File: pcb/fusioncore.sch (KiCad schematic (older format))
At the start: 116 parts, among them J1 40HAT, J10 Pump_Misc_1, J11 Pump_Misc_2, J12 I2C_DBG, J13 Conn_02x03_Top_Bottom, J14 LED, J15 Trigger, J16 WEIGHT, J17 Valve_M1, J18 Valve_M2, J19 Valve_M3, J2 Conn_02x12_Top_Bottom, J20 Valve_M4, J21 Valve_Air_Lime, J22 Valve_Air_Rum, J23 Valve_Air_Out, J3 Flow_Warm, J4 Temperature, J5 Flow_Cold, J6 WEIGHT_B, J7 Pump_Cold, J8 Pump_Warm, J9 Pump_Air, Q1 DMG2305UX, Q10 AO3400A, Q11 AO3400A, Q2 DMMT5401, Q3 AO3400A, Q4 AO3400A, Q5 AO3400A, Q6 AO3400A, Q7 AO3400A, Q8 MMBT4403, Q9 AO3400A, SW1 POWER_ON, U1 CAT24C32, U2 INA226, U3 INA226, U4 INA226, U5 TXB0108DQSR, U6 HX711, U7 P82B96

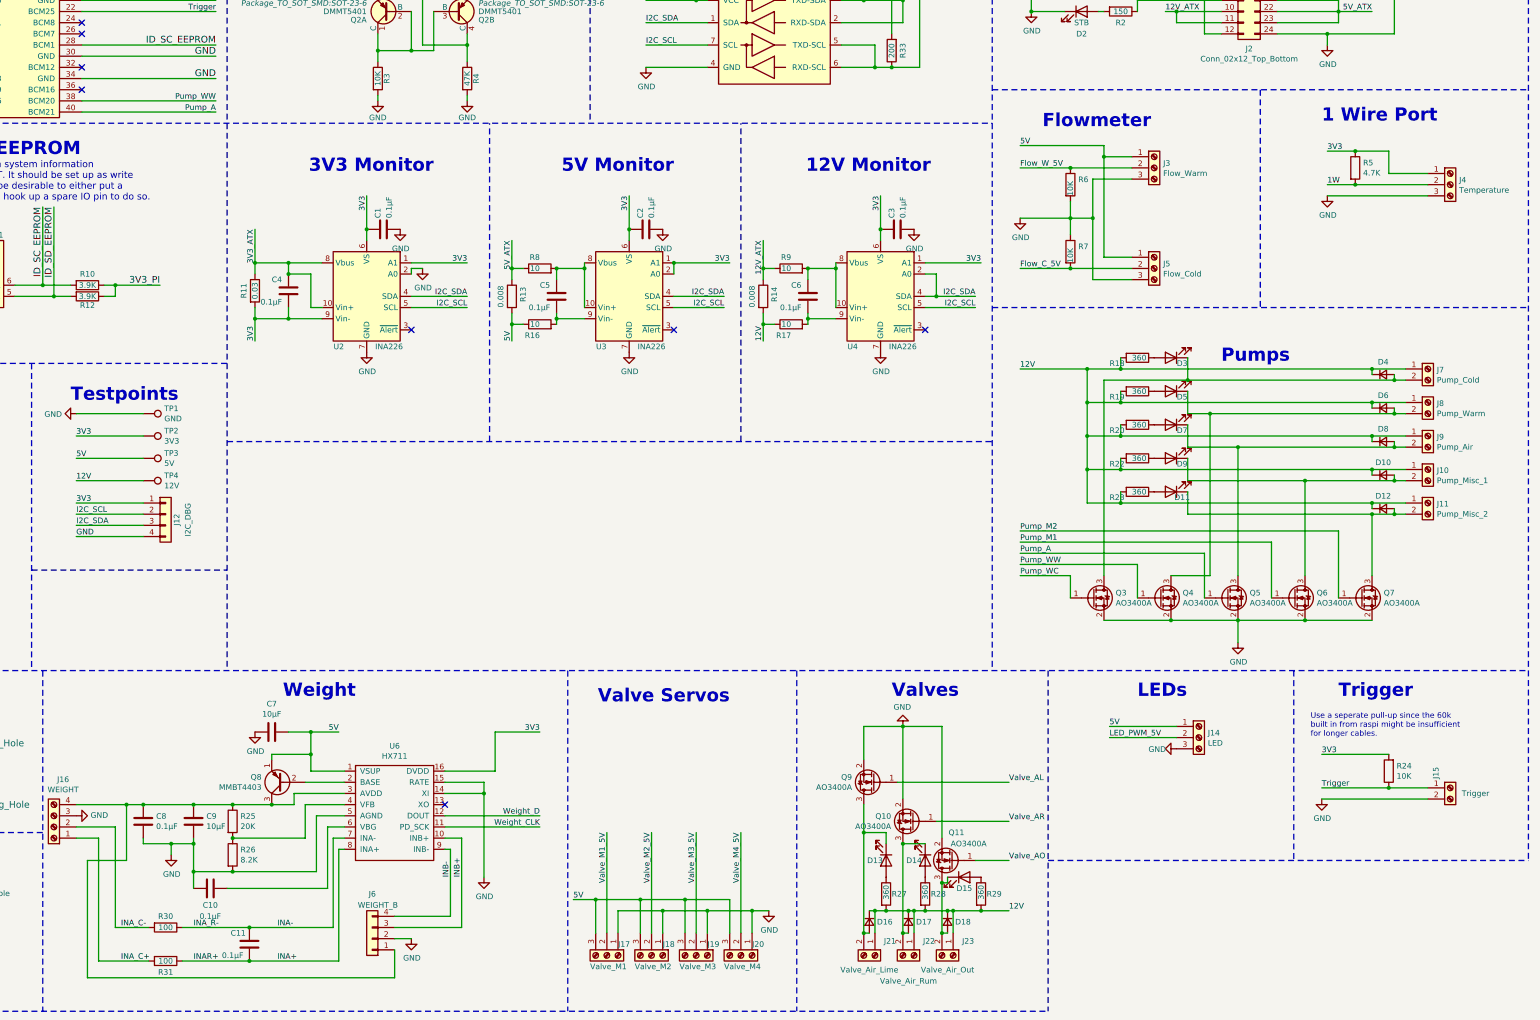
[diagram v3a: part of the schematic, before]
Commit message: Added relais for cooling compressor
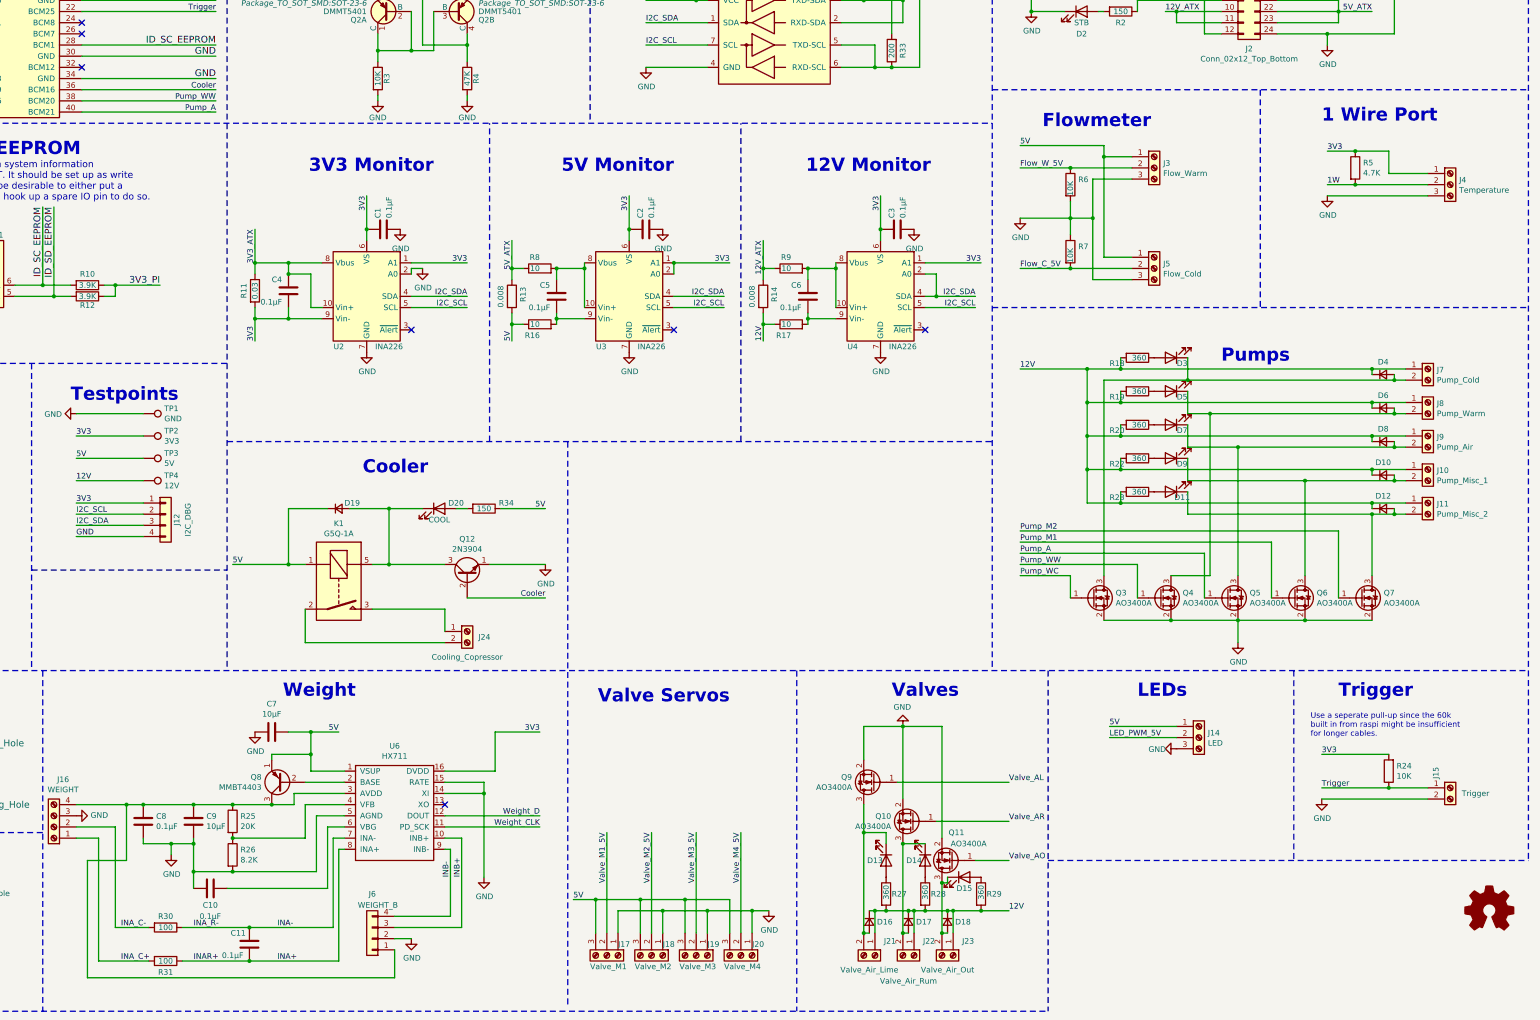
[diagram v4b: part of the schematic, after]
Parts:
- added D19: D, Diode_SMD:D_SMA, symbol Device:D_Small
- added D20: COOL, LED_SMD:LED_0805_2012Metric_Pad1.15x1.40mm_HandSolder, symbol Device:LED
- added J24: Cooling_Copressor, TerminalBlock_Phoenix:TerminalBlock_Phoenix_PT-1,5-2-5.0-H_1x02_P5.00mm_Horizontal, symbol Connector:Screw_Terminal_01x02
- added K1: G5Q-1A, Relay_THT:Relay_SPST_Omron-G5Q-1A, symbol Relay:G5Q-1A
- added Q12: 2N3904, Package_TO_SOT_SMD:SOT-23, symbol Transistor_BJT:2N3904
- added R34: 150, Resistor_SMD:R_0805_2012Metric_Pad1.15x1.40mm_HandSolder, symbol Device:R
- J15: footprint TerminalBlock_Phoenix:TerminalBlock_Phoenix_PT-1,5-2-5.0-H_1x02_P5.00mm_Horizontal -> project_footprints:TerminalBlock_Phoenix_PT-1,5-2-3.5-H_1x02_P3.50mm_Diagonal; Digikey (none) -> 277-1779-ND
- J4: footprint TerminalBlock_Phoenix:TerminalBlock_Phoenix_PT-1,5-3-5.0-H_1x03_P5.00mm_Horizontal -> project_footprints:TerminalBlock_Phoenix_PT-1,5-2-3.5-H_1x03_P3.50mm_Diagonal; Digikey (none) -> 277-1780-ND
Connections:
- net 5V: now also D19.1 (K), K1.1, R34.1
- net GND: now also Q12.1 (E)
- net Cooler: now reaches J1.36 (BCM16)
- net Cooler: now also Q12.2 (B)
- new net: J24.1 (Pin_1), K1.3
- new net: J24.2 (Pin_2), K1.2
- new net: D19.2 (A), D20.1 (K), K1.5, Q12.3 (C)
- new net: D20.2 (A), R34.2
- no-connect marks 13 -> 12
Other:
- note added: "Cooler"
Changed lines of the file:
@@
 F 0 "J4" H 15430 3842 50  0000 L CNN
 F 1 "Temperature" H 15430 3751 50  0000 L CNN
-F 2 "TerminalBlock_Phoenix:TerminalBlock_Phoenix_PT-1,5-3-5.0-H_1x03_P5.00mm_Horizontal" H 15350 3800 50  0001 C CNN
-F 3 "https://media.digikey.com/pdf/Data%20Sheets/Phoenix%20Contact%20PDFs/1935161.pdf" H 15350 3800 50  0001 C CNN
+F 2 "project_footprints:TerminalBlock_Phoenix_PT-1,5-2-3.5-H_1x03_P3.50mm_Diagonal" H 15350 3800 50  0001 C CNN
+F 3 "https://media.digikey.com/pdf/Data%20Sheets/Phoenix%20Contact%20PDFs/Combicon%20Compact%20Series.pdf" H 15350 3800 50  0001 C CNN
+F 4 " 277-1780-ND" H 15350 3800 50  0001 C CNN "Digikey"
 	1    15350 3800
 	1    0    0    -1
@@
 F 0 "J15" V 15222 9280 50  0000 L CNN
 F 1 "Trigger" H 15700 9150 50  0000 R CNN
-F 2 "TerminalBlock_Phoenix:TerminalBlock_Phoenix_PT-1,5-2-5.0-H_1x02_P5.00mm_Horizontal" H 15350 9200 50  0001 C CNN
-F 3 "~" H 15350 9200 50  0001 C CNN
+F 2 "project_footprints:TerminalBlock_Phoenix_PT-1,5-2-3.5-H_1x02_P3.50mm_Diagonal" H 15350 9200 50  0001 C CNN
+F 3 "https://media.digikey.com/pdf/Data%20Sheets/Phoenix%20Contact%20PDFs/Combicon%20Compact%20Series.pdf" H 15350 9200 50  0001 C CNN
+F 4 " 277-1779-ND" V 15350 9200 50  0001 C CNN "Digikey"
 	1    15350 9200
 	1    0    0    -1
@@
 	1900 2950 700  2950
 NoConn ~ 3100 2750
-NoConn ~ 3100 2950
 Wire Wire Line
 	1300 6250 1300 5900
@@
 Wire Notes Line
 	11750 9850 16050 9850
-Wire Notes Line
-	7450 8150 7450 11200
 Wire Notes Line
 	11750 8150 11750 11200
@@
 Wire Wire Line
 	3500 9350 3650 9350
+$Comp
+L Graphic:Logo_Open_Hardware_Small #LOGO1
+U 1 1 5E603C52
+P 15700 10300
+F 0 "#LOGO1" H 15700 10575 50  0001 C CNN
+F 1 "Logo_Open_Hardware_Small" H 15700 10075 50  0001 C CNN
+F 2 "" H 15700 10300 50  0001 C CNN
+F 3 "~" H 15700 10300 50  0001 C CNN
+	1    15700 10300
+	1    0    0    -1
+$EndComp
+$Comp
+L Connector:Screw_Terminal_01x02 J24
+U 1 1 5E60ECEB
+P 6550 7800
+F 0 "J24" H 6650 7750 50  0000 L CNN
+F 1 "Cooling_Copressor" H 6550 7600 50  0000 C TNN
+F 2 "TerminalBlock_Phoenix:TerminalBlock_Phoenix_PT-1,5-2-5.0-H_1x02_P5.00mm_Horizontal" H 6550 7800 50  0001 C CNN
+F 3 "https://media.digikey.com/pdf/Data%20Sheets/Phoenix%20Contact%20PDFs/1935161.pdf" H 6550 7800 50  0001 C CNN
+	1    6550 7800
+	1    0    0    -1
+$EndComp
+Wire Wire Line
+	6350 7900 5100 7900
+Wire Wire Line
+	5100 7900 5100 7600
+$Comp
+L Transistor_BJT:2N3904 Q12
+U 1 1 5E6A5955
+P 6550 7300
+F 0 "Q12" V 6878 7300 50  0000 C CNN
+F 1 "2N3904" V 6787 7300 50  0000 C CNN
+F 2 "Package_TO_SOT_SMD:SOT-23" H 6750 7225 50  0001 L CIN
+F 3 "https://datasheet.lcsc.com/szlcsc/KEC-Semicon-2N3904S-RTK-PS_C18536.pdf" H 6550 7300 50  0001 L CNN
+F 4 "C18536" H 6550 7300 50  0001 C CNN "LCSC"
+	1    6550 7300
+	0    -1   -1   0
+$EndComp
+$Comp
+L Device:D_Small D19
+U 1 1 5E6A8FA4
+P 5400 6700
+F 0 "D19" H 5450 6750 50  0000 L CNN
+F 1 "D" V 5445 6768 50  0001 L CNN
+F 2 "Diode_SMD:D_SMA" V 5400 6700 50  0001 C CNN
+F 3 "~" V 5400 6700 50  0001 C CNN
+F 4 "C22452" V 5400 6700 50  0001 C CNN "LCSC"
+	1    5400 6700
+	1    0    0    -1
+$EndComp
+Wire Wire Line
+	5700 7200 5850 7200
+Wire Wire Line
+	5850 7200 5850 6700
+Wire Wire Line
+	5850 6700 5500 6700
+Wire Wire Line
+	5100 7200 4950 7200
+Wire Wire Line
+	4950 7200 4950 6700
+Wire Wire Line
+	4950 6700 5300 6700
+Wire Wire Line
+	4950 7200 4450 7200
+Connection ~ 4950 7200
+Text Label 4450 7200 0    50   ~ 0
+5V
+Wire Wire Line
+	5850 7200 6350 7200
+Connection ~ 5850 7200
+Wire Wire Line
+	6750 7200 7250 7200
+$Comp
+L power:GND #PWR0103
+U 1 1 5E904F19
+P 7250 7200
+F 0 "#PWR0103" H 7250 6950 50  0001 C CNN
+F 1 "GND" H 7255 7027 50  0000 C CNN
+F 2 "" H 7250 7200 50  0001 C CNN
+F 3 "" H 7250 7200 50  0001 C CNN
+	1    7250 7200
+	1    0    0    -1
+$EndComp
+Wire Wire Line
+	6550 7500 7250 7500
+Text Label 7250 7500 2    50   ~ 0
+Cooler
+$Comp
+L Device:R R34
+U 1 1 5E99FEBD
+P 6700 6700
+F 0 "R34" V 6650 6900 50  0000 C CNN
+F 1 "150" V 6700 6700 50  0000 C CNN
+F 2 "Resistor_SMD:R_0805_2012Metric_Pad1.15x1.40mm_HandSolder" V 6630 6700 50  0001 C CNN
+F 3 "~" H 6700 6700 50  0001 C CNN
+F 4 "C17471" V 6700 6700 50  0001 C CNN "LCSC"
+	1    6700 6700
+	0    1    1    0
+$EndComp
+$Comp
+L Device:LED D20
+U 1 1 5E9A1CDC
+P 6300 6700
+F 0 "D20" H 6450 6750 50  0000 C CNN
+F 1 "COOL" H 6300 6600 50  0000 C CNN
+F 2 "LED_SMD:LED_0805_2012Metric_Pad1.15x1.40mm_HandSolder" H 6300 6700 50  0001 C CNN
+F 3 "~" H 6300 6700 50  0001 C CNN
+F 4 "C2296" H 6300 6700 50  0001 C CNN "LCSC"
+	1    6300 6700
+	1    0    0    -1
+$EndComp
+Wire Wire Line
+	7250 6700 6850 6700
+Wire Wire Line
+	6550 6700 6450 6700
+Wire Wire Line
+	6150 6700 5850 6700
+Connection ~ 5850 6700
+Text Label 7250 6700 2    50   ~ 0
+5V
+Wire Notes Line
+	7450 6100 7450 11150
+Text Notes 6200 6400 2    118  ~ 24
+Cooler
+$Comp
+L Relay:G5Q-1A K1
+U 1 1 5EC7061B
+P 5400 7400
+F 0 "K1" V 4833 7400 50  0000 C CNN
+F 1 "G5Q-1A" V 4924 7400 50  0000 C CNN
+F 2 "Relay_THT:Relay_SPST_Omron-G5Q-1A" H 5750 7350 50  0001 L CNN
+F 3 "https://omronfs.omron.com/en_US/ecb/products/pdf/en-g5q.pdf" H 5400 7400 50  0001 C CNN
+F 4 "Z3632-ND" V 5400 7400 50  0001 C CNN "Digikey"
+	1    5400 7400
+	0    1    1    0
+$EndComp
+Wire Wire Line
+	6350 7600 5700 7600
+Wire Wire Line
+	6350 7600 6350 7800
+Wire Wire Line
+	3100 2950 4300 2950
+Text Label 4300 2950 2    50   ~ 0
+Cooler
 $EndSCHEMATC

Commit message: Added Relais to board
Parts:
- J10, J11, J21, J22, J23, J7, J8, J9: Digikey (none) -> 277-1667-ND
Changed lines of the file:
@@
 F 2 "TerminalBlock_Phoenix:TerminalBlock_Phoenix_PT-1,5-2-5.0-H_1x02_P5.00mm_Horizontal" H 15150 5450 50  0001 C CNN
 F 3 "https://media.digikey.com/pdf/Data%20Sheets/Phoenix%20Contact%20PDFs/1935161.pdf" H 15150 5450 50  0001 C CNN
+F 4 "277-1667-ND" H 15150 5450 50  0001 C CNN "Digikey"
 	1    15150 5450
 	1    0    0    -1
@@
 F 2 "TerminalBlock_Phoenix:TerminalBlock_Phoenix_PT-1,5-2-5.0-H_1x02_P5.00mm_Horizontal" H 15150 5750 50  0001 C CNN
 F 3 "https://media.digikey.com/pdf/Data%20Sheets/Phoenix%20Contact%20PDFs/1935161.pdf" H 15150 5750 50  0001 C CNN
+F 4 "277-1667-ND" H 15150 5750 50  0001 C CNN "Digikey"
 	1    15150 5750
 	1    0    0    -1
@@
 F 2 "TerminalBlock_Phoenix:TerminalBlock_Phoenix_PT-1,5-2-5.0-H_1x02_P5.00mm_Horizontal" H 15150 6050 50  0001 C CNN
 F 3 "https://media.digikey.com/pdf/Data%20Sheets/Phoenix%20Contact%20PDFs/1935161.pdf" H 15150 6050 50  0001 C CNN
+F 4 "277-1667-ND" H 15150 6050 50  0001 C CNN "Digikey"
 	1    15150 6050
 	1    0    0    -1
@@
 F 2 "TerminalBlock_Phoenix:TerminalBlock_Phoenix_PT-1,5-2-5.0-H_1x02_P5.00mm_Horizontal" H 15150 6350 50  0001 C CNN
 F 3 "https://media.digikey.com/pdf/Data%20Sheets/Phoenix%20Contact%20PDFs/1935161.pdf" H 15150 6350 50  0001 C CNN
+F 4 "277-1667-ND" H 15150 6350 50  0001 C CNN "Digikey"
 	1    15150 6350
 	1    0    0    -1
@@
 F 2 "TerminalBlock_Phoenix:TerminalBlock_Phoenix_PT-1,5-2-5.0-H_1x02_P5.00mm_Horizontal" H 15150 6650 50  0001 C CNN
 F 3 "https://media.digikey.com/pdf/Data%20Sheets/Phoenix%20Contact%20PDFs/1935161.pdf" H 15150 6650 50  0001 C CNN
+F 4 "277-1667-ND" H 15150 6650 50  0001 C CNN "Digikey"
 	1    15150 6650
 	1    0    0    -1
@@
 F 2 "TerminalBlock_Phoenix:TerminalBlock_Phoenix_PT-1,5-2-5.0-H_1x02_P5.00mm_Horizontal" H 10900 10700 50  0001 C CNN
 F 3 "https://media.digikey.com/pdf/Data%20Sheets/Phoenix%20Contact%20PDFs/1935161.pdf" H 10900 10700 50  0001 C CNN
+F 4 "277-1667-ND" V 10900 10700 50  0001 C CNN "Digikey"
 	1    10900 10700
 	0    1    1    0
@@
 F 2 "TerminalBlock_Phoenix:TerminalBlock_Phoenix_PT-1,5-2-5.0-H_1x02_P5.00mm_Horizontal" H 10550 10700 50  0001 C CNN
 F 3 "https://media.digikey.com/pdf/Data%20Sheets/Phoenix%20Contact%20PDFs/1935161.pdf" H 10550 10700 50  0001 C CNN
+F 4 "277-1667-ND" V 10550 10700 50  0001 C CNN "Digikey"
 	1    10550 10700
 	0    1    1    0
@@
 F 2 "TerminalBlock_Phoenix:TerminalBlock_Phoenix_PT-1,5-2-5.0-H_1x02_P5.00mm_Horizontal" H 10200 10700 50  0001 C CNN
 F 3 "https://media.digikey.com/pdf/Data%20Sheets/Phoenix%20Contact%20PDFs/1935161.pdf" H 10200 10700 50  0001 C CNN
+F 4 "277-1667-ND" V 10200 10700 50  0001 C CNN "Digikey"
 	1    10200 10700
 	0    1    1    0

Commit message: Added and moved some capacitors
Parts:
- added C12, C13, C14: 0.1μF, Capacitor_SMD:C_0805_2012Metric_Pad1.15x1.40mm_HandSolder, symbol Device:C
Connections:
- net 3V3: now also C13.2, C14.1
- net 5V: now also C12.2
- net GND: now also C12.1, C13.1, C14.2
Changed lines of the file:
@@
 NoConn ~ 3100 2750
 Wire Wire Line
-	1300 6250 1300 5900
-Wire Wire Line
-	1500 6250 1500 5900
+	1300 6250 1300 6200
 Text Label 1300 5900 3    50   ~ 0
 3V3
@@
 	1    0    0    -1
 $EndComp
-Wire Wire Line
-	1000 6250 1000 5900
 Connection ~ 1000 6250
 Text Label 1000 5900 3    50   ~ 0
@@
 Text Label 4300 2950 2    50   ~ 0
 Cooler
+$Comp
+L Device:C C12
+U 1 1 5E7BF599
+P 2100 6100
+F 0 "C12" V 2050 6250 50  0000 R CNN
+F 1 "0.1μF" V 2150 6400 50  0000 R CNN
+F 2 "Capacitor_SMD:C_0805_2012Metric_Pad1.15x1.40mm_HandSolder" H 2138 5950 50  0001 C CNN
+F 3 "~" H 2100 6100 50  0001 C CNN
+F 4 "C49678" H 2100 6100 50  0001 C CNN "LCSC"
+	1    2100 6100
+	0    1    1    0
+$EndComp
+$Comp
+L Device:C C13
+U 1 1 5E869BEF
+P 2100 6350
+F 0 "C13" V 2050 6500 50  0000 R CNN
+F 1 "0.1μF" V 2150 6650 50  0000 R CNN
+F 2 "Capacitor_SMD:C_0805_2012Metric_Pad1.15x1.40mm_HandSolder" H 2138 6200 50  0001 C CNN
+F 3 "~" H 2100 6350 50  0001 C CNN
+F 4 "C49678" H 2100 6350 50  0001 C CNN "LCSC"
+	1    2100 6350
+	0    1    1    0
+$EndComp
+Wire Wire Line
+	1000 5900 1000 6250
+$Comp
+L power:GND #PWR0104
+U 1 1 5E813936
+P 2500 6350
+F 0 "#PWR0104" H 2500 6100 50  0001 C CNN
+F 1 "GND" H 2505 6177 50  0000 C CNN
+F 2 "" H 2500 6350 50  0001 C CNN
+F 3 "" H 2500 6350 50  0001 C CNN
+	1    2500 6350
+	1    0    0    -1
+$EndComp
+Wire Wire Line
+	2250 6100 2500 6100
+Wire Wire Line
+	2500 6100 2500 6350
+Wire Wire Line
+	1500 5900 1500 6100
+Wire Wire Line
+	2250 6350 2500 6350
+Connection ~ 2500 6350
+Wire Wire Line
+	1950 6100 1500 6100
+Connection ~ 1500 6100
+Wire Wire Line
+	1500 6100 1500 6250
+Wire Wire Line
+	1950 6350 1850 6350
+Wire Wire Line
+	1850 6350 1850 6200
+Wire Wire Line
+	1850 6200 1300 6200
+Connection ~ 1300 6200
+Wire Wire Line
+	1300 6200 1300 5900
+$Comp
+L Device:C C14
+U 1 1 5EA9FECD
+P 6650 8700
+F 0 "C14" V 6600 8850 50  0000 R CNN
+F 1 "0.1μF" V 6800 8850 50  0000 R CNN
+F 2 "Capacitor_SMD:C_0805_2012Metric_Pad1.15x1.40mm_HandSolder" H 6688 8550 50  0001 C CNN
+F 3 "~" H 6650 8700 50  0001 C CNN
+F 4 "C49678" H 6650 8700 50  0001 C CNN "LCSC"
+	1    6650 8700
+	0    1    1    0
+$EndComp
+Connection ~ 6800 8700
+$Comp
+L power:GND #PWR0105
+U 1 1 5EAA3D3D
+P 6400 8700
+F 0 "#PWR0105" H 6400 8450 50  0001 C CNN
+F 1 "GND" H 6405 8527 50  0000 C CNN
+F 2 "" H 6400 8700 50  0001 C CNN
+F 3 "" H 6400 8700 50  0001 C CNN
+	1    6400 8700
+	1    0    0    -1
+$EndComp
+Wire Wire Line
+	6500 8700 6400 8700
 $EndSCHEMATC

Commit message: Added LCSC for R30/R31
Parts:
- R30, R31: LCSC (none) -> C17408
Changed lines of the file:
@@
 F 2 "Resistor_SMD:R_0805_2012Metric_Pad1.15x1.40mm_HandSolder" V 3780 10450 50  0001 C CNN
 F 3 "~" H 3850 10450 50  0001 C CNN
+F 4 "C17408" V 3850 10450 50  0001 C CNN "LCSC"
 	1    3850 10450
 	0    1    1    0
@@
 F 2 "Resistor_SMD:R_0805_2012Metric_Pad1.15x1.40mm_HandSolder" V 3780 10750 50  0001 C CNN
 F 3 "~" H 3850 10750 50  0001 C CNN
+F 4 "C17408" V 3850 10750 50  0001 C CNN "LCSC"
 	1    3850 10750
 	0    1    1    0
